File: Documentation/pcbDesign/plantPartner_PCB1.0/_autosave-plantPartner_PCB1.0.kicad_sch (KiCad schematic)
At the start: 26 parts, among them IC1 MPM3610, J1 Conn_01x04, J2 Conn_01x04, J3 Conn_01x04, J4 Screw_Terminal, J5 Screw_Terminal, J6 Screw_Terminal, U1 ESP32-WROOM-32, U2 MAX485

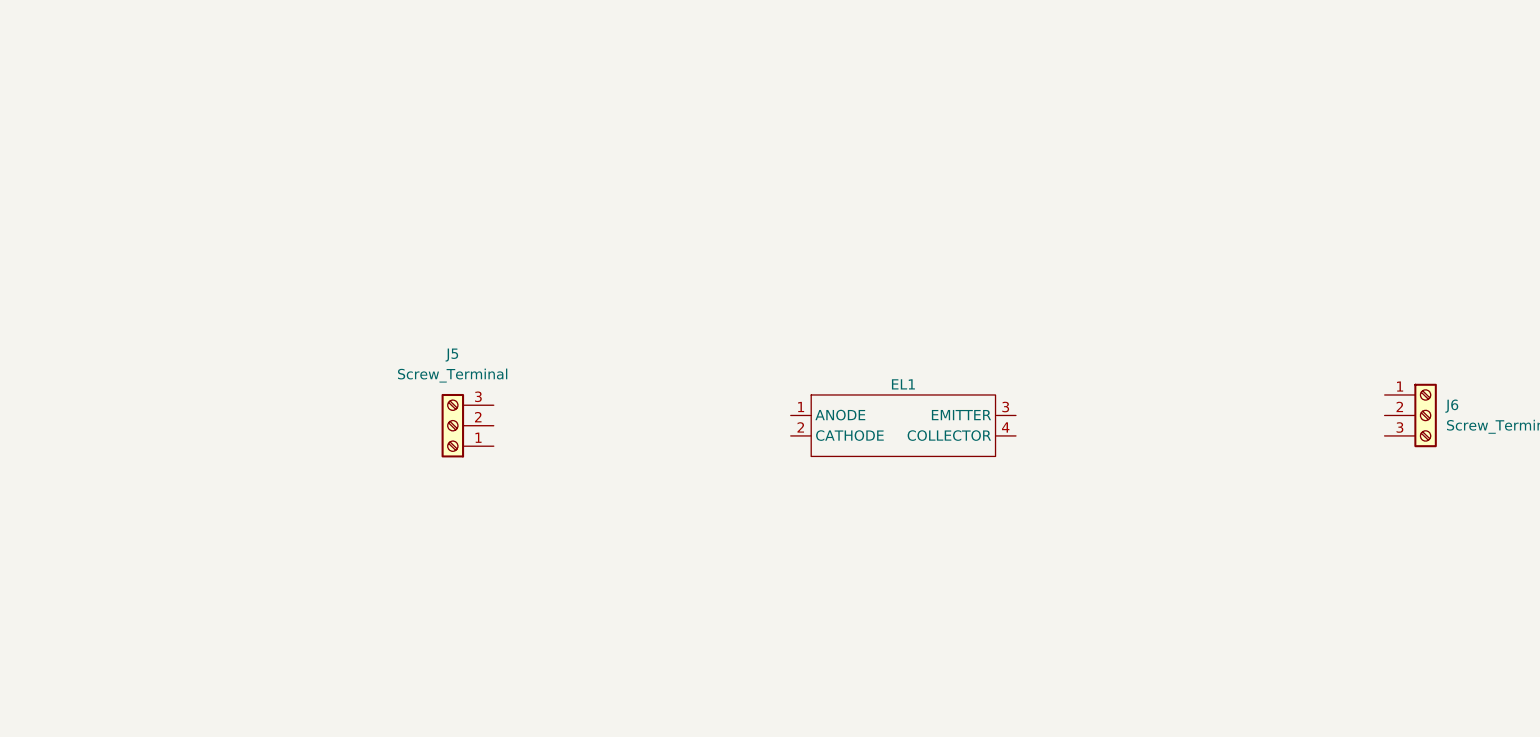
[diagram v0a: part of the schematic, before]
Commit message: Added RS485 Transceiver and progressed with ESP32 and 12V Relay
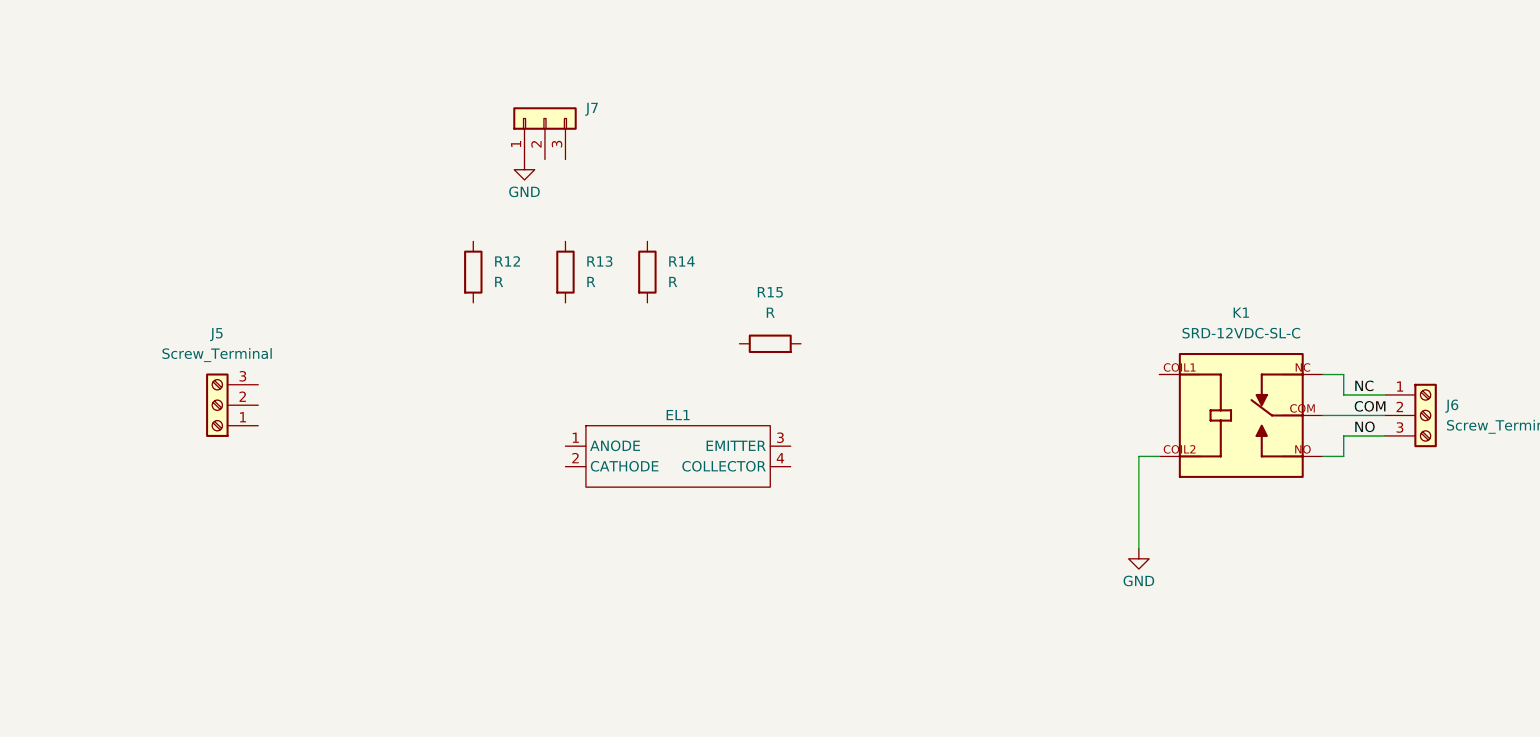
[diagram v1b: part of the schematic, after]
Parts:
- added J7: Conn_01x03, symbol Connector_Generic:Conn_01x03
- added K1: SRD-12VDC-SL-C, SRD-12VDC-SL-C:RELAY_SRD-12VDC-SL-C, symbol SRD-12VDC-SL-C:SRD-12VDC-SL-C
- added R12, R13, R14, R15: R, Resistor_SMD:R_0201_0603Metric, symbol Device:R
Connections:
- net GND: now also J7.1 (Pin_1), K1.COIL2
- net NC: now reaches J6.1 (Pin_1)
- net NC: now also K1.NC
- net COM: now reaches J6.2 (Pin_2)
- net COM: now also K1.COM
- net NO: now reaches J6.3 (Pin_3)
- net NO: now also K1.NO
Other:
- moved on the sheet: EL1, J5
